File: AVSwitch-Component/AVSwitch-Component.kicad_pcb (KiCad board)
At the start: 2 copper layers, 100 x 100 mm, 11 parts, among them J1 Conn_01x35_Pin, U1 SN74CBT3244PW

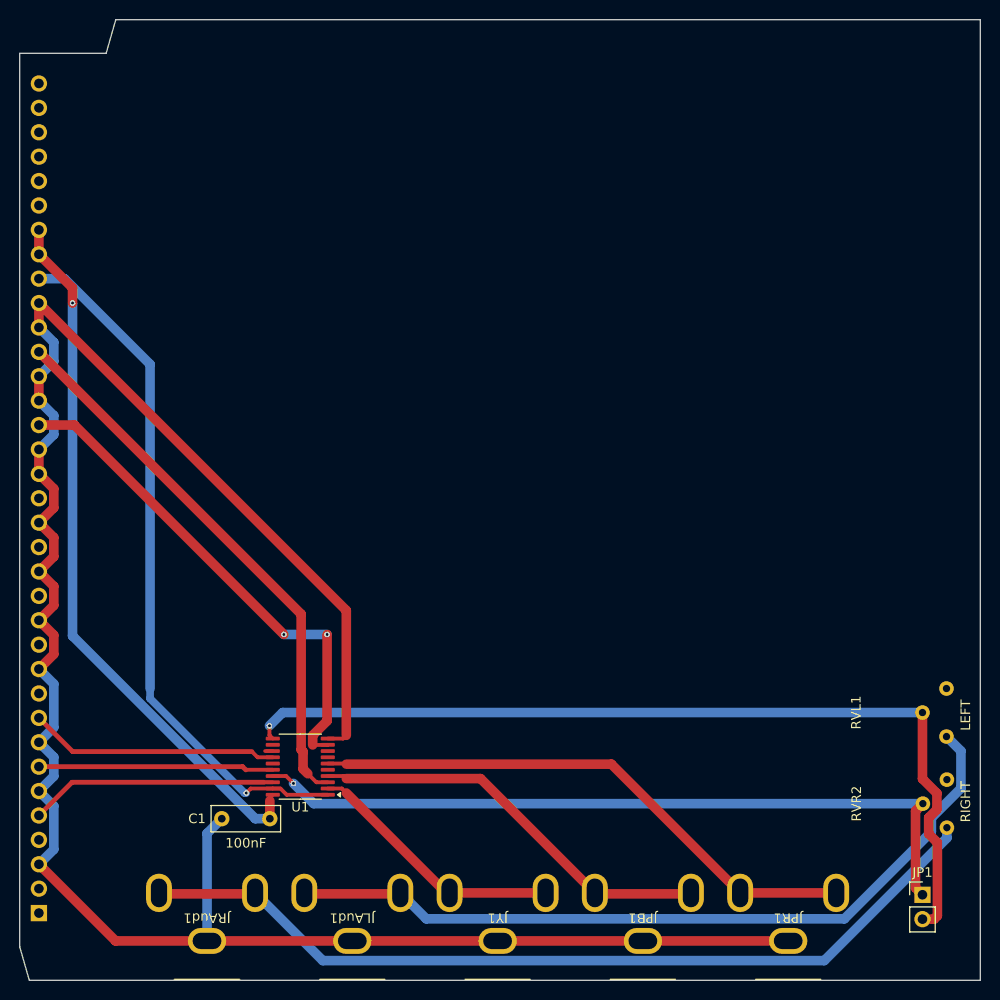
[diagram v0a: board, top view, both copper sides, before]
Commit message: Add files via upload
New version with better footprint and ground isolation.
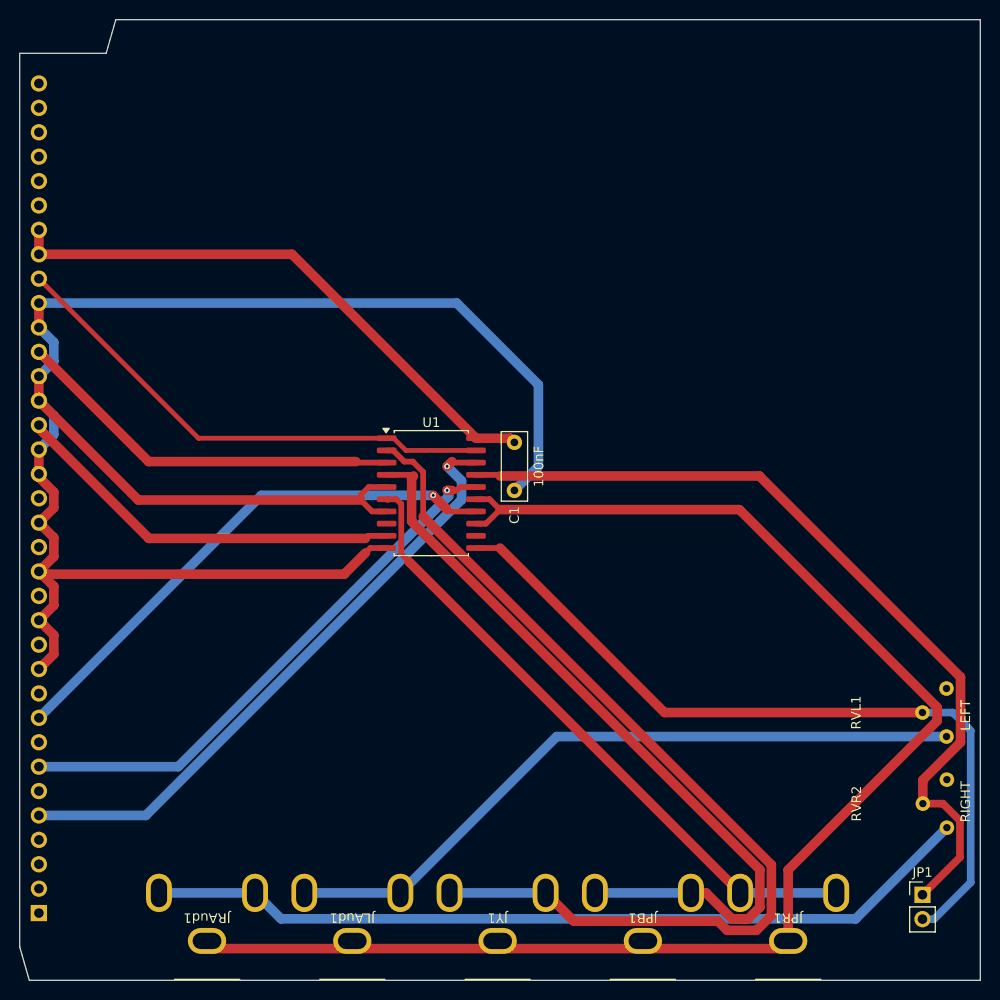
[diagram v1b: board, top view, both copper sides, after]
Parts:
- U1: footprint Package_SO:TSSOP-20_4.4x6.5mm_P0.65mm -> Package_SO:SOIC-20W_7.5x12.8mm_P1.27mm
- moved C1 46.7 mm to (157.5, 91.0), turned to -90 degrees
- moved U1 31.6 mm to (148.8, 96.3), turned to 0 degrees
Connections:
- JLAud1 pad 2: GND -> Net-(JLAud1-Ext)
- JPB1 pad 2: GND -> Net-(JLAud1-Ext)
- JPR1 pad 2: GND -> Net-(JLAud1-Ext)
- JRAud1 pad 2: GND -> Net-(JLAud1-Ext)
- JY1 pad 2: GND -> Net-(JLAud1-Ext)
- U1 pad 13: unconnected-(U1-2A2-Pad13) -> Net-(JLAud1-Ext)
- U1 pad 15: unconnected-(U1-2A3-Pad15) -> Net-(JLAud1-Ext)
- U1 pad 5: unconnected-(U1-2B3-Pad5) -> GND
- U1 pad 7: unconnected-(U1-2B2-Pad7) -> GND
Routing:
- net Net-(JLAud1-Ext): track 0.00 -> 152.0 mm
- net Net-(JY1-In): track 27.2 -> 101.7 mm
- net /CV_Y: track 25.8 -> 65.0 mm, vias 0 -> 1
- net Net-(JPB1-In): track 42.8 -> 81.6 mm
- net /CV_Pb: track 24.5 -> 58.1 mm, vias 0 -> 1
- net /CV_Pr: track 26.0 -> 55.8 mm, vias 0 -> 1
- net GND: track 224.8 -> 195.3 mm
- net /ACTIVE: track 73.1 -> 52.9 mm, vias 1 -> 0
- net /R_AUD: track 58.0 -> 41.0 mm
- net +5V: track 74.8 -> 60.2 mm, vias 1 -> 0
- net Net-(JP1-B): track 94.2 -> 81.8 mm, vias 1 -> 0
- net /L_AUD: track 52.7 -> 41.4 mm, vias 2 -> 0
- net Net-(JP1-A): track 79.0 -> 87.9 mm, vias 1 -> 0
- net Net-(JPR1-In): track 58.5 -> 66.9 mm
- net Net-(JLAud1-In): track 82.0 -> 73.6 mm
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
